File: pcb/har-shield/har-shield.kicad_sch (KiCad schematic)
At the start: 0 parts

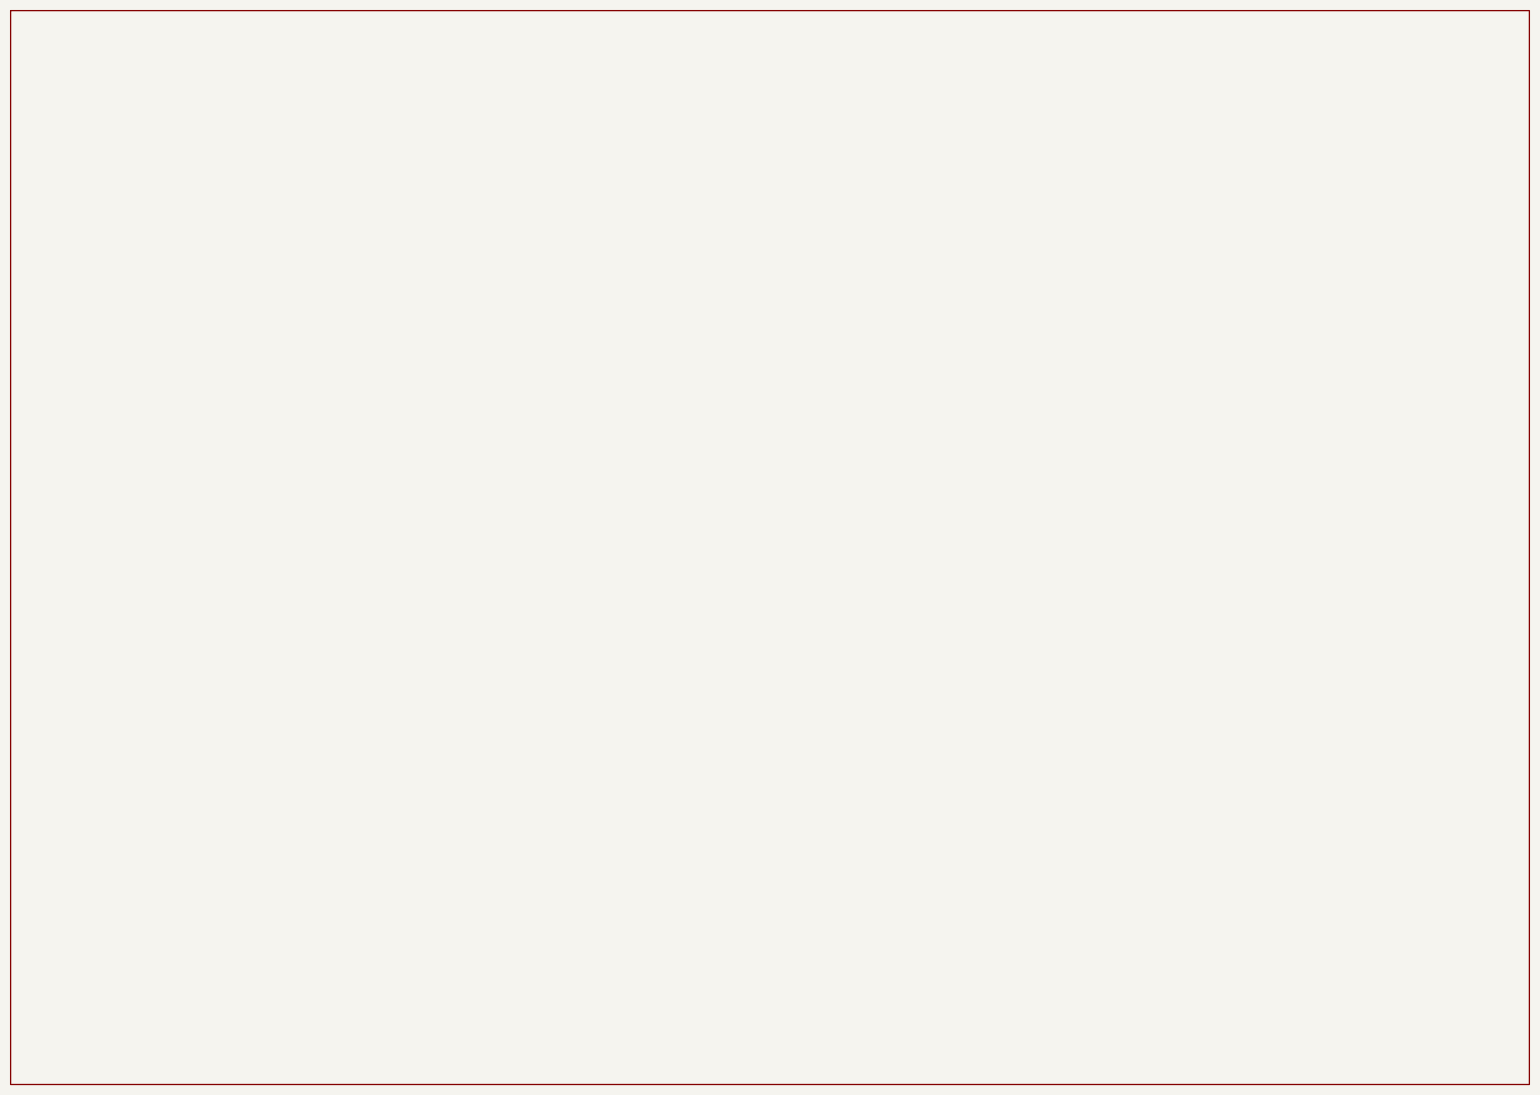
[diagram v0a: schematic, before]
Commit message: D1-PCB: 手动完成ESP32-S3原理图 (IO17=SDA/IO18=SCL, GY-521+GY-273)
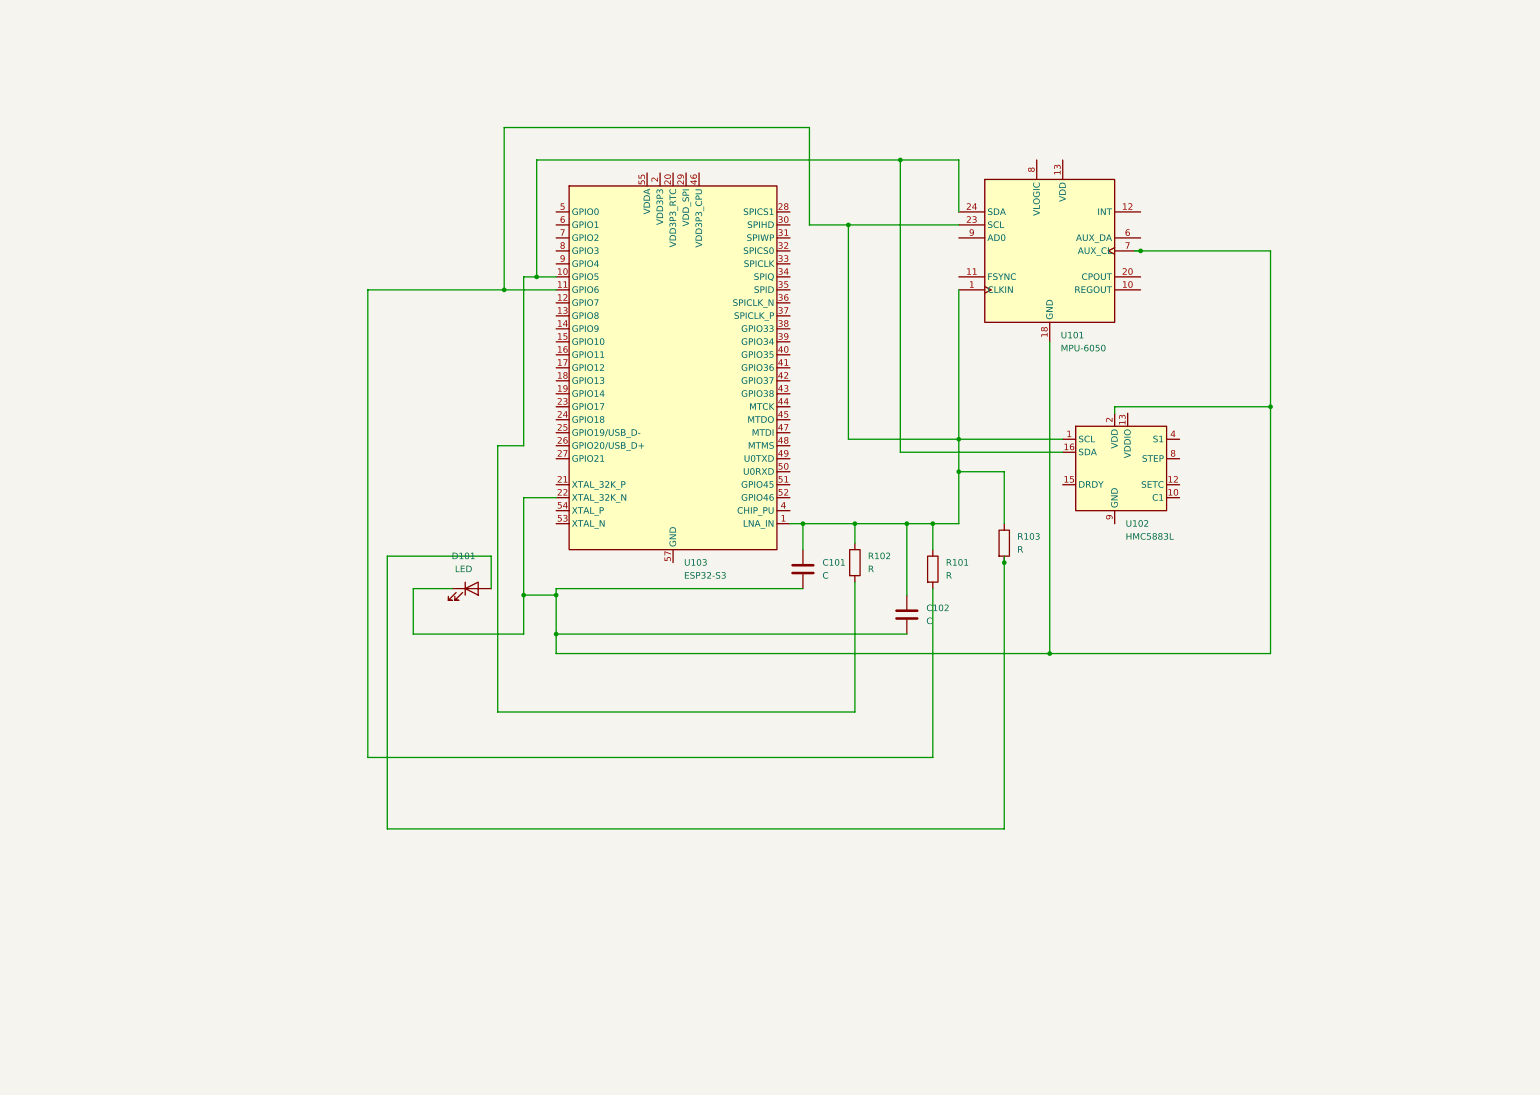
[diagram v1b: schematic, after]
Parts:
- added C101, C102: C, symbol Device:C
- added D101: LED, symbol Device:LED
- added R101, R102, R103: R, symbol Device:R
- added U101: MPU-6050, Sensor_Motion:InvenSense_QFN-24_4x4mm_P0.5mm, symbol Sensor_Motion:MPU-6050
- added U102: HMC5883L, Library:LGA-16_3x3mm_P0.5mm, symbol Library:HMC5883L
- added U103: ESP32-S3, Package_DFN_QFN:QFN-56-1EP_7x7mm_P0.4mm_EP4x4mm, symbol MCU_Espressif:ESP32-S3
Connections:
- new net: C101.1, C102.1, R101.1, R101.2, R102.1, R103.1, U101.1 (CLKIN), U101.23 (SCL), U102.1 (SCL), U103.1 (LNA_IN), U103.11 (GPIO6)
- new net: C101.2, C102.2, D101.1 (K), U101.18 (GND), U101.7 (AUX_CL), U102.2 (VDD), U103.22 (XTAL_32K_N)
- new net: R102.2, U101.24 (SDA), U102.16 (SDA), U103.10 (GPIO5)
- new net: U102.11 (GND), U102.9 (GND)
- new net: U102.14 (NC), U102.3 (NC), U102.5 (NC), U102.6 (NC), U102.7 (NC)
- new net: U103.2 (VDD3P3), U103.3 (VDD3P3)
- new net: U103.55 (VDDA), U103.56 (VDDA)
- new net: D101.2 (A), R103.2
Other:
- removed sheet ?
- company: HAR Project -> (none)
- title: ESP32-S3 HAR Sensor Shield -> (none)

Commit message: D2: GY-521 six-position calibration + MicroPython firmware
- calib/calibrate.py: six-position accel, ellipsoid mag, Allan variance
- calib/process_mpu6050_calib.py: serial data → calib_params.json + plots
- calib/capture_mpu6050.py: pySerial capture script (bypass Thonny buffer)
- calib/calib_params.json: real GY-521 params (bias/scale/gyro/Allan coeffs)
- firmware/mpu6050_calib/main.py: MicroPython REPL-based calibration firmware
- firmware/har_firmware.ino: Arduino backup (MPU6050+HMC5883L)
- reports/标定报告.md: methods, measured params, Allan noise, comparison charts
- reports/figures/: accel_calib, allan_accel, allan_gyro (real data)
- D2/: delivery package (params + report + figures + raw/calibrated datasets)
- PROJECT_STATUS.md, TODO.md: updated project tracking
- pcb/: user's manual schematic + PCB, gen_sch.py removed
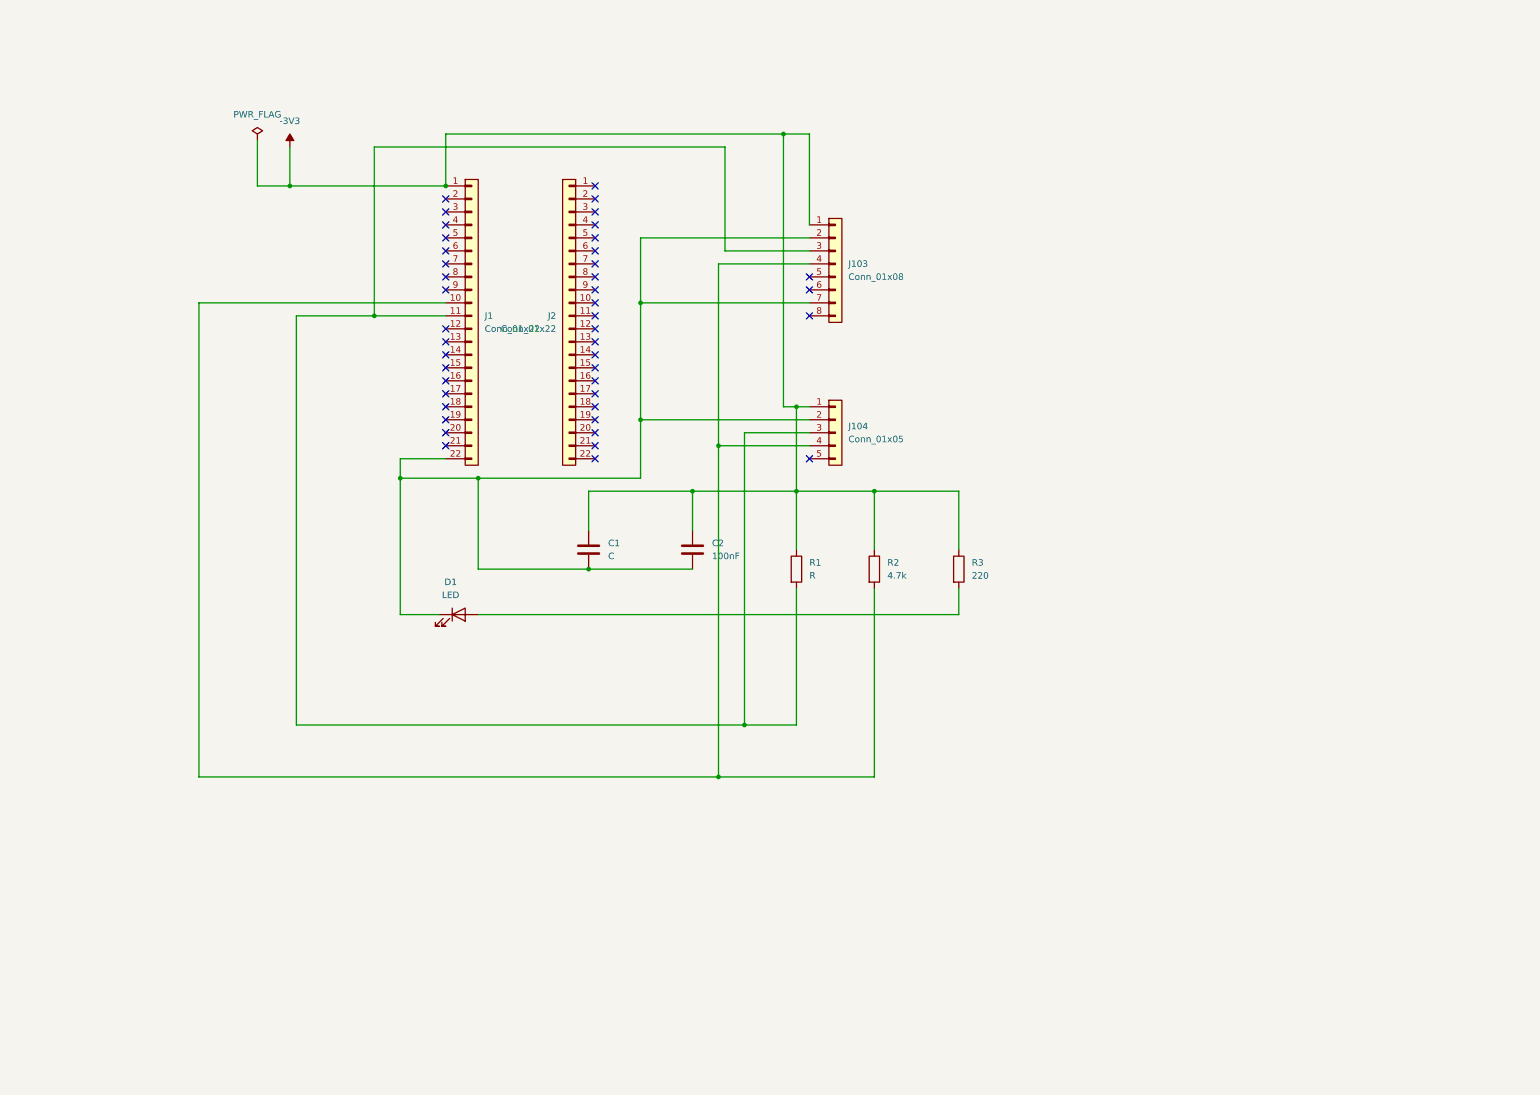
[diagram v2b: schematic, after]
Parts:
- removed U101: MPU-6050, Sensor_Motion:InvenSense_QFN-24_4x4mm_P0.5mm, symbol Sensor_Motion:MPU-6050
- removed U102: HMC5883L, Library:LGA-16_3x3mm_P0.5mm, symbol Library:HMC5883L
- removed U103: ESP32-S3, Package_DFN_QFN:QFN-56-1EP_7x7mm_P0.4mm_EP4x4mm, symbol MCU_Espressif:ESP32-S3
- added J1, J2: Conn_01x22, Connector_PinHeader_2.54mm:PinHeader_1x22_P2.54mm_Vertical, symbol Connector_Generic:Conn_01x22
- added J103: Conn_01x08, Connector_PinHeader_2.54mm:PinHeader_1x08_P2.54mm_Vertical, symbol Connector_Generic:Conn_01x08
- added J104: Conn_01x05, Connector_PinHeader_2.54mm:PinHeader_1x05_P2.54mm_Vertical, symbol Connector_Generic:Conn_01x05
- C1: renamed from C101; footprint (none) -> Capacitor_SMD:C_0805_2012Metric
- C2: renamed from C102; value C -> 100nF; footprint (none) -> Capacitor_SMD:C_0805_2012Metric
- D1: renamed from D101; footprint (none) -> LED_SMD:LED_0805_2012Metric
- R1: renamed from R101; footprint (none) -> Resistor_SMD:R_0805_2012Metric
- R2: renamed from R102; value R -> 4.7k; footprint (none) -> Resistor_SMD:R_0805_2012Metric
- R3: renamed from R103; value R -> 220; footprint (none) -> Resistor_SMD:R_0805_2012Metric
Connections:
- net -3V3: now reaches C1.1, C2.1, R1.1, R2.1, R3.1
- net -3V3: now also J1.1 (Pin_1), J103.1 (Pin_1), J104.1 (Pin_1); no longer R1.2
- net at C1.2, C2.2, D1.1 (K): now also J1.22 (Pin_22), J103.2 (Pin_2), J103.7 (Pin_7), J104.2 (Pin_2)
- net at R2.2: now also J1.10 (Pin_10), J103.4 (Pin_4), J104.4 (Pin_4)
- new net: J1.11 (Pin_11), J103.3 (Pin_3), J104.3 (Pin_3), R1.2
- no-connect marks 0 -> 44
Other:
- moved on the sheet: C1, C2, D1, R1, R2, R3
